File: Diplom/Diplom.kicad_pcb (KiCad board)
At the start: 2 copper layers, 100 x 80.1 mm, 91 parts, among them IC1 E22-900T22D, J1 Conn_01x02_Pin, J2 Conn_01x05_Pin, J3 Conn_01x02_Pin, Q1 SI2301, SW1 SW_Push, SW2 SW_Push, U2 BME280, U3 W25Q32JVSS, U4 SPV1040, U5 DW01A, U6 STM32F411CEUx, Y3 ABM3-25.000MHz-D2Y-T, Y4 KX-327NHT, Y5 Crystal

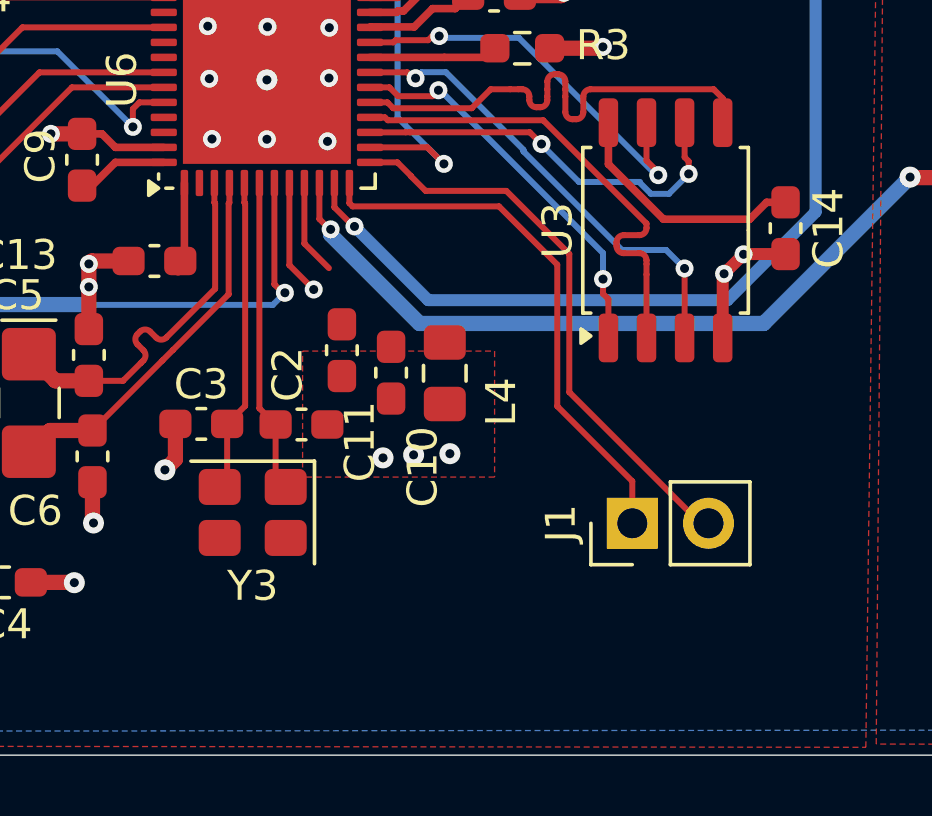
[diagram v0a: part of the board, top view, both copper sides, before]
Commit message: Add gitmodule, corrections
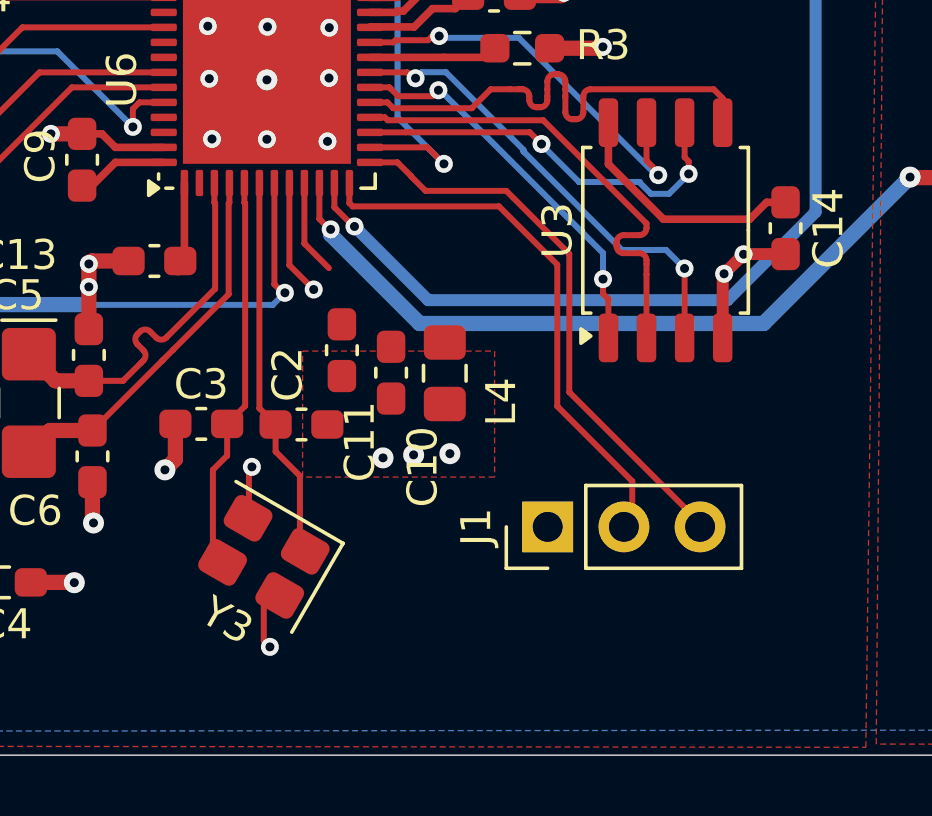
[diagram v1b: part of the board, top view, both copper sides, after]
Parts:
- J1: value Conn_01x02_Pin -> Conn_01x03_Pin; footprint Connector_PinHeader_2.54mm:PinHeader_1x02_P2.54mm_Vertical -> Connector_PinHeader_2.54mm:PinHeader_1x03_P2.54mm_Vertical
- moved J1 2.82 mm to (119.6, 99.2)
- moved Y3 1.53 mm to (110.1, 100.2), turned to 150 degrees
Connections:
- J1 pad 1: /MCU/USART2_TX -> GND
- J1 pad 2: /MCU/USART2_RX -> /MCU/USART2_TX
- Y3 pad 2: /MCU/OSC_N -> GND
- Y3 pad 3: (no net) -> /MCU/OSC_N
- Y3 pad 4: (no net) -> GND
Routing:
- net GND: track 92.6 -> 96.1 mm, vias 69 -> 71
- net /MCU/OSC_N: track 10.5 -> 12.8 mm
- net /MCU/OSC_P: track 10.5 -> 12.7 mm
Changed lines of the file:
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@@
 		)
 	)
-	(footprint "Connector_PinHeader_2.54mm:PinHeader_1x02_P2.54mm_Vertical"
+	(footprint "Connector_PinHeader_2.54mm:PinHeader_1x03_P2.54mm_Vertical"
 		(layer "F.Cu")
-		(at 122.38 99.08 90)
-		(descr "Through hole straight pin header, 1x02, 2.54mm pitch, single row")
-		(tags "Through hole pin header THT 1x02 2.54mm single row")
+		(at 119.560001 99.2 90)
+		(descr "Through hole straight pin header, 1x03, 2.54mm pitch, single row")
+		(tags "Through hole pin header THT 1x03 2.54mm single row")
 		(property "Reference" "J1"
 			(at 0 -2.38 90)
@@
 			)
 		)
-		(property "Value" "Conn_01x02_Pin"
-			(at 0 4.919999 90)
+		(property "Value" "Conn_01x03_Pin"
+			(at 0 7.460001 90)
 			(layer "F.Fab")
 			(effects
@@
 			)
 		)
-		(property "Description" "Generic connector, single row, 01x02, script generated"
+		(property "Description" "Generic connector, single row, 01x03, script generated"
 			(at 0 0 90)
 			(layer "F.Fab")
@@
 		(fp_line
 			(start 1.38 1.27)
-			(end 1.38 3.92)
+			(end 1.38 6.46)
 			(stroke
 				(width 0.12)
@@
 		(fp_line
 			(start -1.38 1.27)
-			(end -1.38 3.92)
+			(end -1.38 6.46)
 			(stroke
 				(width 0.12)
@@
 		)
 		(fp_line
-			(start -1.38 3.92)
-			(end 1.38 3.92)
+			(start -1.38 6.46)
+			(end 1.38 6.46)
 			(stroke
 				(width 0.12)
@@
 		(fp_line
 			(start -1.77 -1.77)
-			(end -1.77 4.32)
+			(end -1.77 6.849999)
 			(stroke
 				(width 0.05)
@@
 		)
 		(fp_line
-			(start 1.77 4.32)
+			(start 1.77 6.849999)
 			(end 1.77 -1.77)
 			(stroke
@@
 		)
 		(fp_line
-			(start -1.77 4.32)
-			(end 1.77 4.32)
+			(start -1.77 6.849999)
+			(end 1.77 6.849999)
 			(stroke
 				(width 0.05)
@@
 		(fp_line
 			(start 1.27 -1.27)
-			(end 1.27 3.81)
+			(end 1.270001 6.35)
 			(stroke
 				(width 0.1)
@@
 		)
 		(fp_line
-			(start 1.27 3.81)
-			(end -1.27 3.81)
+			(start 1.270001 6.35)
+			(end -1.270001 6.35)
 			(stroke
 				(width 0.1)
@@
 		)
 		(fp_line
-			(start -1.27 3.81)
+			(start -1.270001 6.35)
 			(end -1.27 -0.635)
 			(stroke
@@
 		)
 		(fp_text user "${REFERENCE}"
-			(at 0 1.270001 0)
+			(at 0 2.54 0)
 			(layer "F.Fab")
 			(effects
@@
 			(layers "*.Cu" "*.Mask")
 			(remove_unused_layers no)
-			(net 74 "/MCU/USART2_TX")
+			(net 3 "GND")
 			(pinfunction "Pin_1")
 			(pintype "passive")
@@
 			(layers "*.Cu" "*.Mask")
 			(remove_unused_layers no)
-			(net 64 "/MCU/USART2_RX")
+			(net 74 "/MCU/USART2_TX")
 			(pinfunction "Pin_2")
 			(pintype "passive")
 		)
+		(pad "3" thru_hole circle
+			(at 0 5.079999 90)
+			(size 1.7 1.7)
+			(drill 1)
+			(layers "*.Cu" "*.Mask")
+			(remove_unused_layers no)
+			(net 64 "/MCU/USART2_RX")
+			(pinfunction "Pin_3")
+			(pintype "passive")
+		)
 		(embedded_fonts no)
-		(model "${KICAD9_3DMODEL_DIR}/Connector_PinHeader_2.54mm.3dshapes/PinHeader_1x02_P2.54mm_Vertical.step"
+		(model "${KICAD9_3DMODEL_DIR}/Connector_PinHeader_2.54mm.3dshapes/PinHeader_1x03_P2.54mm_Vertical.step"
 			(offset
 				(xyz 0 0 0)
@@
 	(footprint "Crystal:Crystal_SMD_3225-4Pin_3.2x2.5mm"
 		(layer "F.Cu")
-		(at 109.7268 98.7189 180)
+		(at 110.1 100.2 150)
 		(descr "SMD3225/4, Crystal, 3.2x2.5mm package, SMD, generated with kicad-footprint-generator make_crystal.py, http://www.txccrystal.com/images/pdf/7m-accuracy.pdf")
 		(property "Reference" "Y3"
-			(at 0 -2.450001 0)
+			(at -0.000001 -2.450002 150)
 			(layer "F.SilkS")
 			(effects
@@
 		)
 		(property "Value" "ABM3-25.000MHz-D2Y-T"
-			(at 0 2.450001 0)
+			(at 0.000001 2.450002 150)
 			(layer "F.Fab")
 			(effects
@@
 		)
 		(property "Datasheet" "~"
-			(at 0 0 0)
+			(at 0 0 150)
 			(layer "F.Fab")
 			(hide yes)
@@
 			)
 		)
-		(property "Description" "Two pin crystal 8 MHz"
-			(at 0 0 0)
+		(property "Description" "Four pin crystal, GND on pins 2 and 4"
+			(at 0 0 150)
 			(layer "F.Fab")
 			(hide yes)
@@
 		(attr smd)
 		(fp_line
-			(start -2.06 1.710001)
-			(end 2.06 1.710001)
+			(start -2.059999 -1.71)
+			(end -2.059999 1.71)
 			(stroke
 				(width 0.12)
@@
 		)
 		(fp_line
-			(start -2.06 -1.710001)
-			(end -2.06 1.710001)
+			(start -2.059999 1.71)
+			(end 2.059999 1.71)
 			(stroke
 				(width 0.12)
@@
 		(fp_poly
 			(pts
-				(xy -2.1 -1.75) (xy -2.1 1.75) (xy 2.1 1.75) (xy 2.1 -1.75)
+				(xy -2.099999 -1.75) (xy -2.1 1.749999) (xy 2.099999 1.75) (xy 2.1 -1.749999)
 			)
 			(stroke
@@
 		(fp_poly
 			(pts
-				(xy -1.6 -1.25) (xy -1.6 0.625) (xy -0.975001 1.25) (xy 1.6 1.25) (xy 1.6 -1.25)
+				(xy -1.599999 -1.25) (xy -1.600001 0.625001) (xy -0.975 1.250001) (xy 1.599999 1.25) (xy 1.599999 -1.25)
 			)
 			(stroke
@@
 		)
 		(fp_text user "${REFERENCE}"
-			(at 0 0 0)
+			(at 0 0 150)
 			(layer "F.Fab")
 			(effects
@@
 		)
 		(pad "1" smd roundrect
-			(at -1.1 0.85 180)
+			(at -1.1 0.85 150)
 			(size 1.4 1.2)
 			(layers "F.Cu" "F.Mask" "F.Paste")
@@
 		)
 		(pad "2" smd roundrect
-			(at 1.1 0.85 180)
+			(at 1.1 0.849999 150)
 			(size 1.4 1.2)
 			(layers "F.Cu" "F.Mask" "F.Paste")
 			(roundrect_rratio 0.208333)
-			(net 73 "/MCU/OSC_N")
+			(net 3 "GND")
 			(pinfunction "2")
 			(pintype "passive")
 		)
 		(pad "3" smd roundrect
-			(at 1.1 -0.85 180)
+			(at 1.1 -0.85 150)
 			(size 1.4 1.2)
 			(layers "F.Cu" "F.Mask" "F.Paste")
 			(roundrect_rratio 0.208333)
+			(net 73 "/MCU/OSC_N")
+			(pinfunction "3")
+			(pintype "passive")
 		)
 		(pad "4" smd roundrect
-			(at -1.1 -0.85 180)
+			(at -1.1 -0.849999 150)
 			(size 1.4 1.2)
 			(layers "F.Cu" "F.Mask" "F.Paste")
 			(roundrect_rratio 0.208333)
+			(net 3 "GND")
+			(pinfunction "4")
+			(pintype "passive")
 		)
 		(embedded_fonts no)
@@
 	)
 	(segment
+		(start 109.6 98.697919)
+		(end 109.6 97.3)
+		(width 0.2)
+		(layer "F.Cu")
+		(net 3)
+	)
+	(segment
 		(start 137.33 58.810001)
 		(end 137.585 58.555001)
@@
 	)
 	(segment
+		(start 109.6 97.3)
+		(end 109.7 97.2)
+		(width 0.2)
+		(layer "F.Cu")
+		(net 3)
+	)
+	(segment
 		(start 72.84 82.39)
 		(end 72.87 82.42)
@@
 	)
 	(segment
+		(start 110.09628 101.558204)
+		(end 110.09628 102.99628)
+		(width 0.2)
+		(layer "F.Cu")
+		(net 3)
+	)
+	(segment
 		(start 72.84 84.617499)
 		(end 72.84 82.45)
@@
 	)
 	(segment
+		(start 110.09628 102.99628)
+		(end 110.3 103.2)
+		(width 0.2)
+		(layer "F.Cu")
+		(net 3)
+	)
+	(segment
 		(start 110.95 90.4775)
 		(end 111.76 91.2875)
@@
 	)
 	(segment
+		(start 109.723223 98.821142)
+		(end 109.6 98.697919)
+		(width 0.2)
+		(layer "F.Cu")
+		(net 3)
+	)
+	(segment
 		(start 69.91 83.37)
 		(end 70.89 82.39)
@@
 	)
 	(via
+		(at 109.7 97.2)
+		(size 0.6)
+		(drill 0.3)
+		(layers "F.Cu" "B.Cu")
+		(net 3)
+	)
+	(via
 		(at 137.585 58.555001)
 		(size 0.7)
@@
 	)
 	(via
+		(at 110.3 103.2)
+		(size 0.6)
+		(drill 0.3)
+		(layers "F.Cu" "B.Cu")
+		(net 3)
+	)
+	(via
 		(at 120.1 81.4)
 		(size 0.6)
@@
 	)
 	(segment
-		(start 110.49 97.532101)
-		(end 110.8268 97.8689)
+		(start 109.95 87.7375)
+		(end 109.95 95.2475)
 		(width 0.2)
 		(layer "F.Cu")
@@
 	)
 	(segment
-		(start 109.95 87.7375)
-		(end 109.95 95.2475)
+		(start 110.49 95.7875)
+		(end 110.49 96.69)
+		(width 0.2)
+		(layer "F.Cu")
+		(net 72)
+	)
+	(segment
+		(start 110.49 96.69)
+		(end 111.3 97.5)
+		(width 0.2)
+		(layer "F.Cu")
+		(net 72)
+	)
+	(segment
+		(start 111.3 97.5)
+		(end 111.3 99.836251)
 		(width 0.2)
 		(layer "F.Cu")
@@
 	)
 	(segment
-		(start 110.49 95.7875)
-		(end 110.49 97.532101)
+		(start 108.4 100.063749)
+		(end 108.4 97.3)
 		(width 0.2)
 		(layer "F.Cu")
-		(net 72)
+		(net 73)
 	)
 	(segment
-		(start 108.875001 97.620699)
-		(end 108.6268 97.8689)
+		(start 109.475 95.167501)
+		(end 109.475 88.418751)
 		(width 0.2)
 		(layer "F.Cu")
@@
 	)
 	(segment
-		(start 109.475 88.418751)
-		(end 109.475 95.167501)
+		(start 109.45 88.393751)
+		(end 109.449999 87.7375)
 		(width 0.2)
 		(layer "F.Cu")
@@
 	)
 	(segment
-		(start 109.449999 87.7375)
-		(end 109.45 88.393751)
+		(start 108.875001 95.7675)
+		(end 109.475 95.167501)
 		(width 0.2)
 		(layer "F.Cu")
@@
 	)
 	(segment
-		(start 109.45 88.393751)
-		(end 109.475 88.418751)
+		(start 109.475 88.418751)
+		(end 109.45 88.393751)
 		(width 0.2)
 		(layer "F.Cu")
@@
 	)
 	(segment
-		(start 109.475 95.167501)
-		(end 108.875001 95.7675)
+		(start 108.4 97.3)
+		(end 108.875003 96.824997)
 		(width 0.2)
 		(layer "F.Cu")
@@
 	)
 	(segment
-		(start 108.875001 95.7675)
-		(end 108.875001 97.620699)
+		(start 108.875003 96.824997)
+		(end 108.875003 95.7675)
 		(width 0.2)
 		(layer "F.Cu")
